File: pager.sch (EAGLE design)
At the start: 62 parts, among them Q1 25 MHz, Q2 SI2333DS, SW1 CHS-01A1, SW2 CHS-01A1, U1 VOCORE2SMD, U2 VOCORE2SMD, U3 XR22800IL, X1 52745-3090

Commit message: Fixed some parts, better placement
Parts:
- C11: value 18 pF -> 4.7 uF cer; device pager:CAP_CERAMIC_0402 -> pager:CAP_CERAMIC_0603
- C9: value 4.7 uF cer -> 18 pF; device pager:CAP_CERAMIC_0603 -> pager:CAP_CERAMIC_0402
- R1, R10, R25: value 50 -> 10 k
- R17: value 226 -> 50
- R18: value 1M -> 50
- R19: value 40.2k -> 50
- R20: value 10 k -> 50
- R36: value 50 -> 1M
- R37: value 10 k -> 226
- R38: value 10 k -> 40.2k
- U1, U2: value VOCORE2SMD -> VOCORE2-SMD; device pager:VOCORE2SMD -> pager:VOCORE2-SMD
- X1: value 52745-3090 -> OMRON_XF2L-30REVERSE; device pager:52745-3090 -> pager:OMRON_XF2L-30REVERSE
- X2: value (none) -> FCI_8193_MICRO_USB; device pager:USB"" -> pager:FCI_8193_MICRO_USB
- renumbered WP_CORE to TP2, WP_WIFI to TP1
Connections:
- removed net BIAS_1B: C9.1, U3.+3.3V_OUT, U3.CAP1, U3.CAP2
- removed net N$26: X2.GND
- new net 3.3V_USB: C11.1, U3.+3.3V_OUT, U3.CAP1, U3.CAP2
- net +5V: now also C13.1; no longer C12.1, U1.+5.0VI_2, U2.+5.0VI_2
- net 3.3_CORE: now also R13.2, R15.2, R17.2, R19.2, R21.2, R23.2, R26.2, U2.+3.3VO; no longer R1.2, R10.2, R12.2, R2.2, R3.2, R4.2, R9.2, U1.+3.3VO, U1.+3.3VO_2, U1.+3.3VO_3
- net 3.3_WIFI: now also R2.2, R4.2, R6.2, R8.2, U1.+3.3VO; no longer R13.2, R14.2, R15.2, R16.2, U2.+3.3VO, U2.+3.3VO_2, U2.+3.3VO_3
- net DISP_RESET: now also R25.2, U2.(GPIO#39)EPHY_LED4_N_JTRST_N; no longer R20.2, U1.(GPIO#39)EPHY_LED4_N_JTRST_N
- net DISP_RX0: now also U2.(GPIO#45,PWM_CH0)UART_TXD1; no longer U1.(GPIO#45,PWM_CH0)UART_TXD1
- net DISP_TX0: now also U2.(GPIO#46,PWM_CH1)UART_RXD1; no longer U1.(GPIO#46,PWM_CH1)UART_RXD1
- net ETH_1A_RX_N: now also C8.1, R19.1, R20.2, U2.MDI_RN_P0; no longer C4.1, R21.2, R4.1, U1.MDI_RN_P0
- net ETH_1A_RX_P: now also C7.1, R21.1, U2.MDI_RP_P0; no longer C3.1, R3.1, U1.MDI_RP_P0
- net ETH_1A_TX_N: now also C6.1, R23.1, R24.2, U2.MDI_TN_P0; no longer C2.1, R2.1, R23.2, U1.MDI_TN_P0
- net ETH_1A_TX_P: now also C5.1, R26.1, R27.2, U2.MDI_TP_P0; no longer C1.1, R1.1, R24.2, U1.MDI_TP_P0
- net ETH_1B_RX_N: now also C6.2, R30.1, R31.2; no longer C2.2, R26.2, R6.1
- net ETH_1B_RX_P: now also C5.2, R28.1, R29.2; no longer C1.2, R25.2, R5.1
- net ETH_1B_TX_N: now also C8.2, R34.1, R35.2; no longer C4.2, R28.2, R8.1
- net ETH_1B_TX_P: now also C7.2, R32.1, R33.2; no longer C3.2, R27.2, R7.1
- net ETH_2A_RX_N: now also C4.1, R17.1, R18.2, U2.(PWM_CH1,GPIO#19,SD_D6)MDI_RN_P2; no longer C8.1, R12.1, R32.2, U1.(PWM_CH1,GPIO#19,SD_D6)MDI_RN_P2
- net ETH_2A_RX_P: now also C3.1, R15.1, R16.2, U2.(PWM_CH0,GPIO#18,SD_D7)MDI_RP_P2; no longer C7.1, R11.1, R31.2, U1.(PWM_CH0,GPIO#18,SD_D7)MDI_RP_P2
- net ETH_2A_TX_N: now also C2.1, R13.1, R14.2, U2.(UART_RXD2,GPIO#21,PWM_CH3,SD_D4)MDI_TN_P2; no longer C6.1, R10.1, R30.2, U1.(UART_RXD2,GPIO#21,PWM_CH3,SD_D4)MDI_TN_P2
- net ETH_2A_TX_P: now also C1.1, R11.1, R12.2, U2.(UART_TXD2,GPIO#20,PWM_CH2,SD_D5)MDI_TP_P2; no longer C5.1, R29.2, R9.1, U1.(UART_TXD2,GPIO#20,PWM_CH2,SD_D5)MDI_TP_P2
- net ETH_2B_RX_N: now also C2.2, R6.1, R7.2, U1.MDI_RN_P0; no longer C6.2, R14.1, R35.2, U2.MDI_RN_P0
- net ETH_2B_RX_P: now also C1.2, R8.1, R9.2, U1.MDI_RP_P0; no longer C5.2, R13.1, R36.2, U2.MDI_RP_P0
- net ETH_2B_TX_N: now also C4.2, R2.1, R3.2, U1.MDI_TN_P0; no longer C8.2, R16.1, R33.2, U2.MDI_TN_P0
- net ETH_2B_TX_P: now also C3.2, R4.1, R5.2, U1.MDI_TP_P0; no longer C7.2, R15.1, R34.2, U2.MDI_TP_P0
- net GND: now also C11.2, C13.2, C9.1, R1.1, R10.1, R12.1, R14.1, R16.1, R18.1, R3.1, R5.1, R7.1, R9.1, X2.GND; no longer C11.1, C12.2, C9.2, R17.1, R19.1, R21.1, R23.1, R26.1, R28.1, R30.1, R32.1, R34.1, R36.1, U1.GND_2, U1.GND_3, U1.GND_4, U1.GND_5, U1.GND_6, U1.GND_7, U2.GND_2, U2.GND_3, U2.GND_4, U2.GND_5, U2.GND_6, U2.GND_7
- net N$10: now also R28.2, R30.2, R32.2, R34.2; no longer R5.2, R6.2, R7.2, R8.2
- net N$21: now also R37.2; no longer R17.2
- net N$22: now also C10.2, R36.2; no longer C11.2, R18.2
- net N$23: now also C9.2, R36.1; no longer C10.2, R18.1
- net N$27: now also C12.1; no longer C13.1
- net N$28: now also C12.2, R38.2; no longer C13.2, R19.2
- net WP_CORE: now also R10.2; no longer R38.2
- net WP_WIFI: now also R1.2; no longer R37.2
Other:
- moved on the sheet: C1, C10, C11, C12, C13, C2, C3, C4, C5, C6, C7, C8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

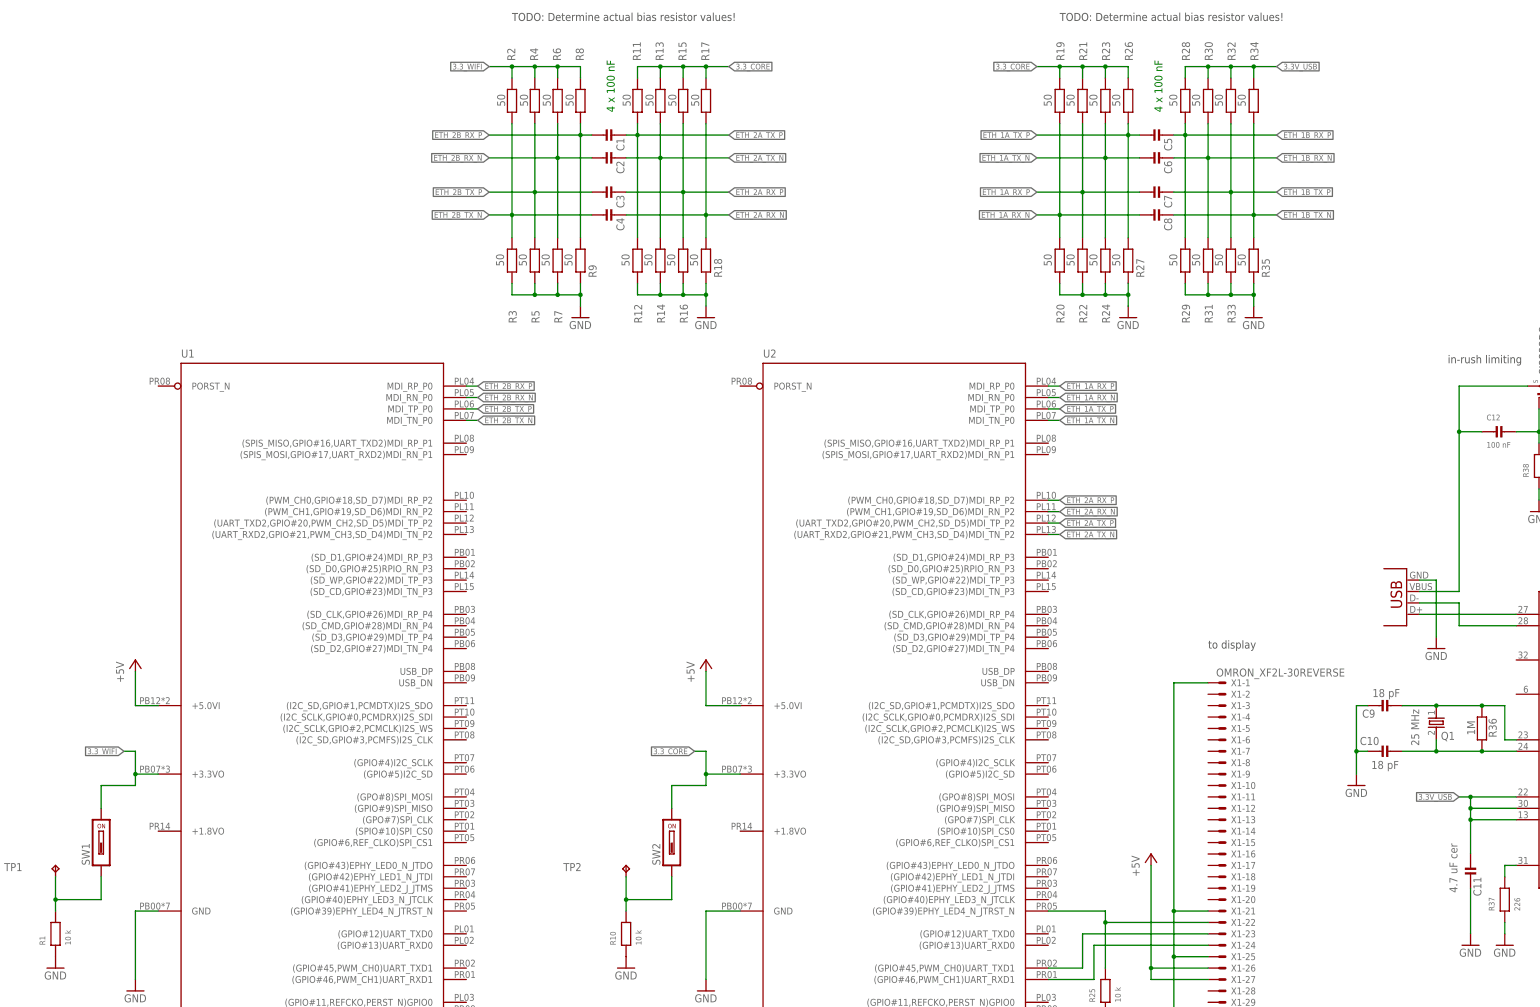
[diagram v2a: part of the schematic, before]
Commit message: Added wifi_reset wire, polygons on tRestrict for Vocore's and routed power bus and USB
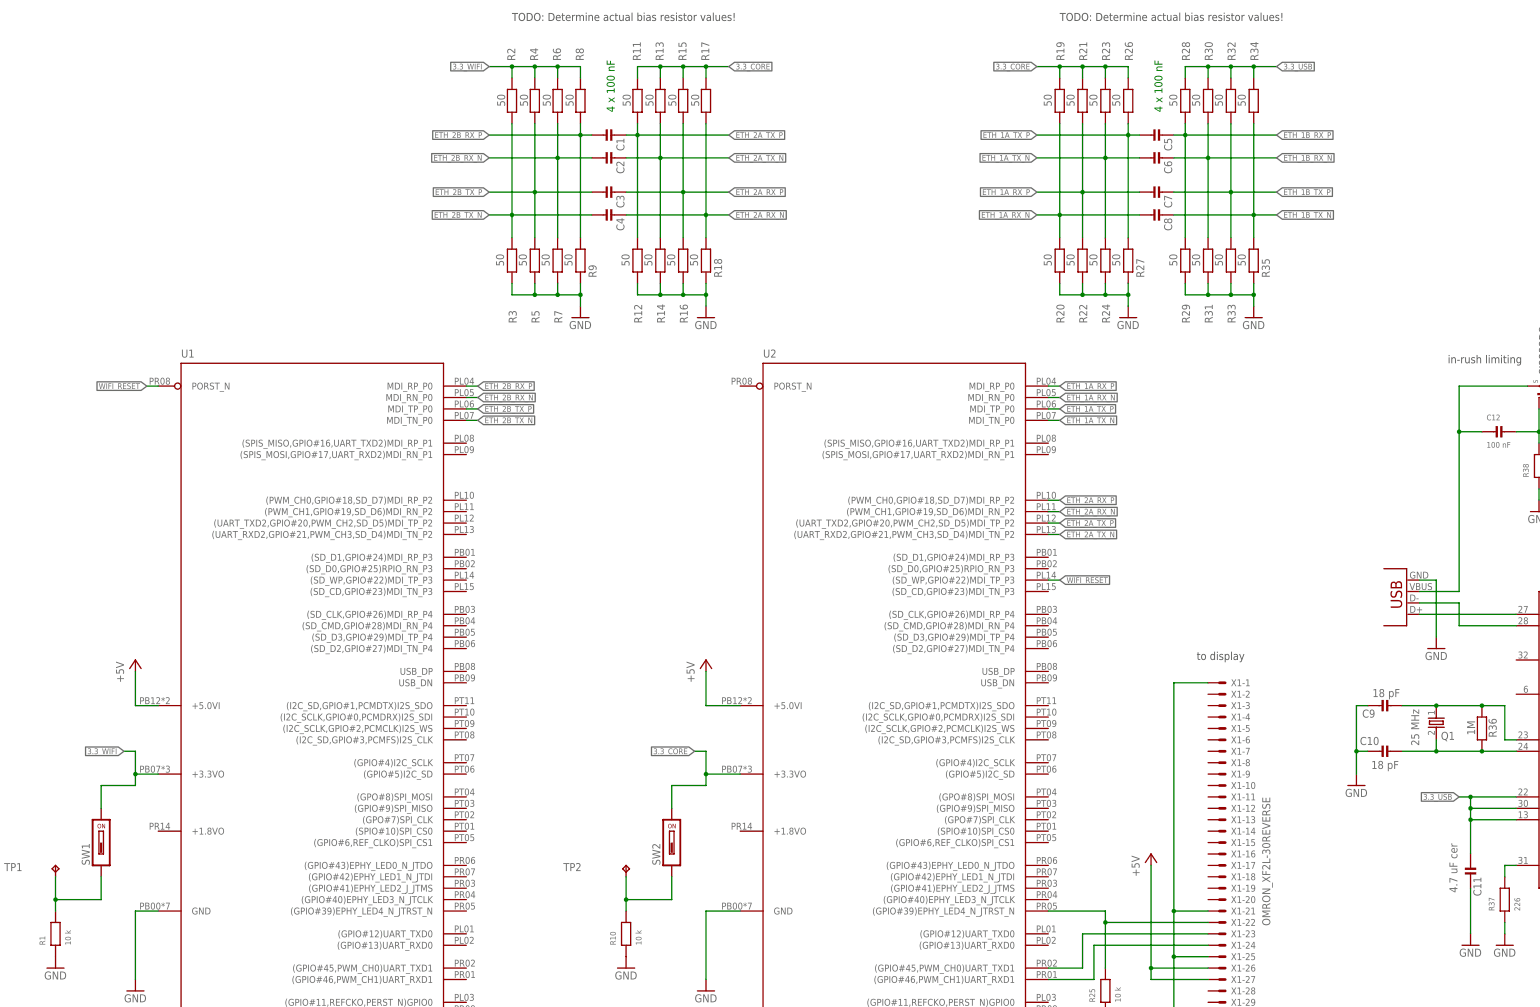
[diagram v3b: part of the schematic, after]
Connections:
- removed net 3.3V_USB: C11.1, U3.+3.3V_OUT, U3.CAP1, U3.CAP2
- removed net N$10: R28.2, R30.2, R32.2, R34.2
- new net 3.3_USB: C11.1, R28.2, R30.2, R32.2, R34.2, U3.+3.3V_OUT, U3.CAP1, U3.CAP2
- new net WIFI_RESET: U1.PORST_N, U2.(SD_WP,GPIO#22)MDI_TP_P3

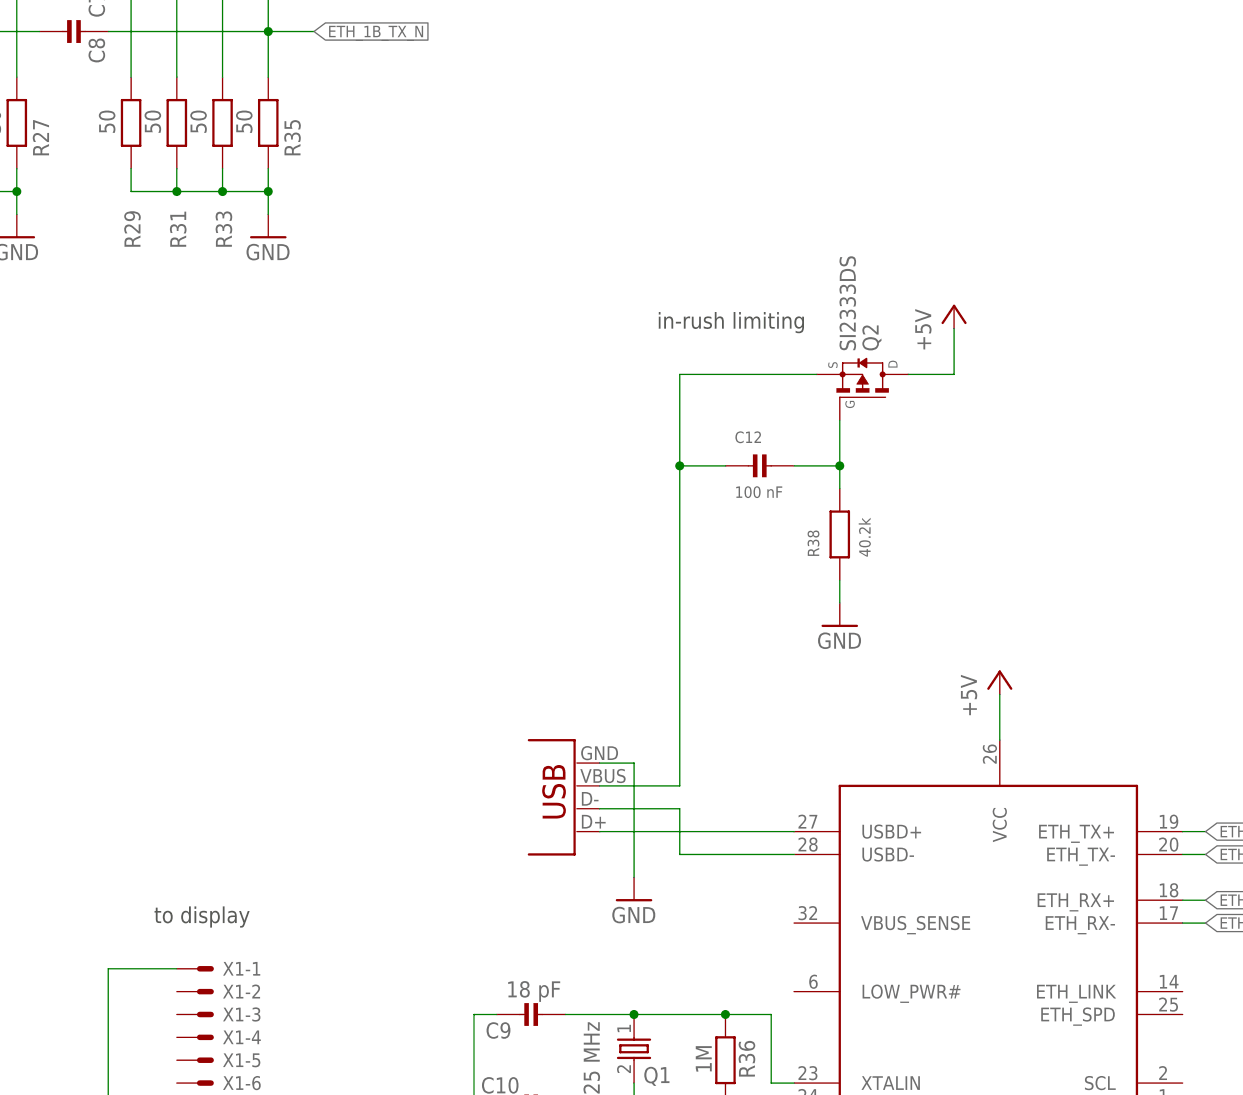
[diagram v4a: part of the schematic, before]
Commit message: Added TVS, resistor and cap between USB-shield and GND, made +5V bus 0.8 mm thick
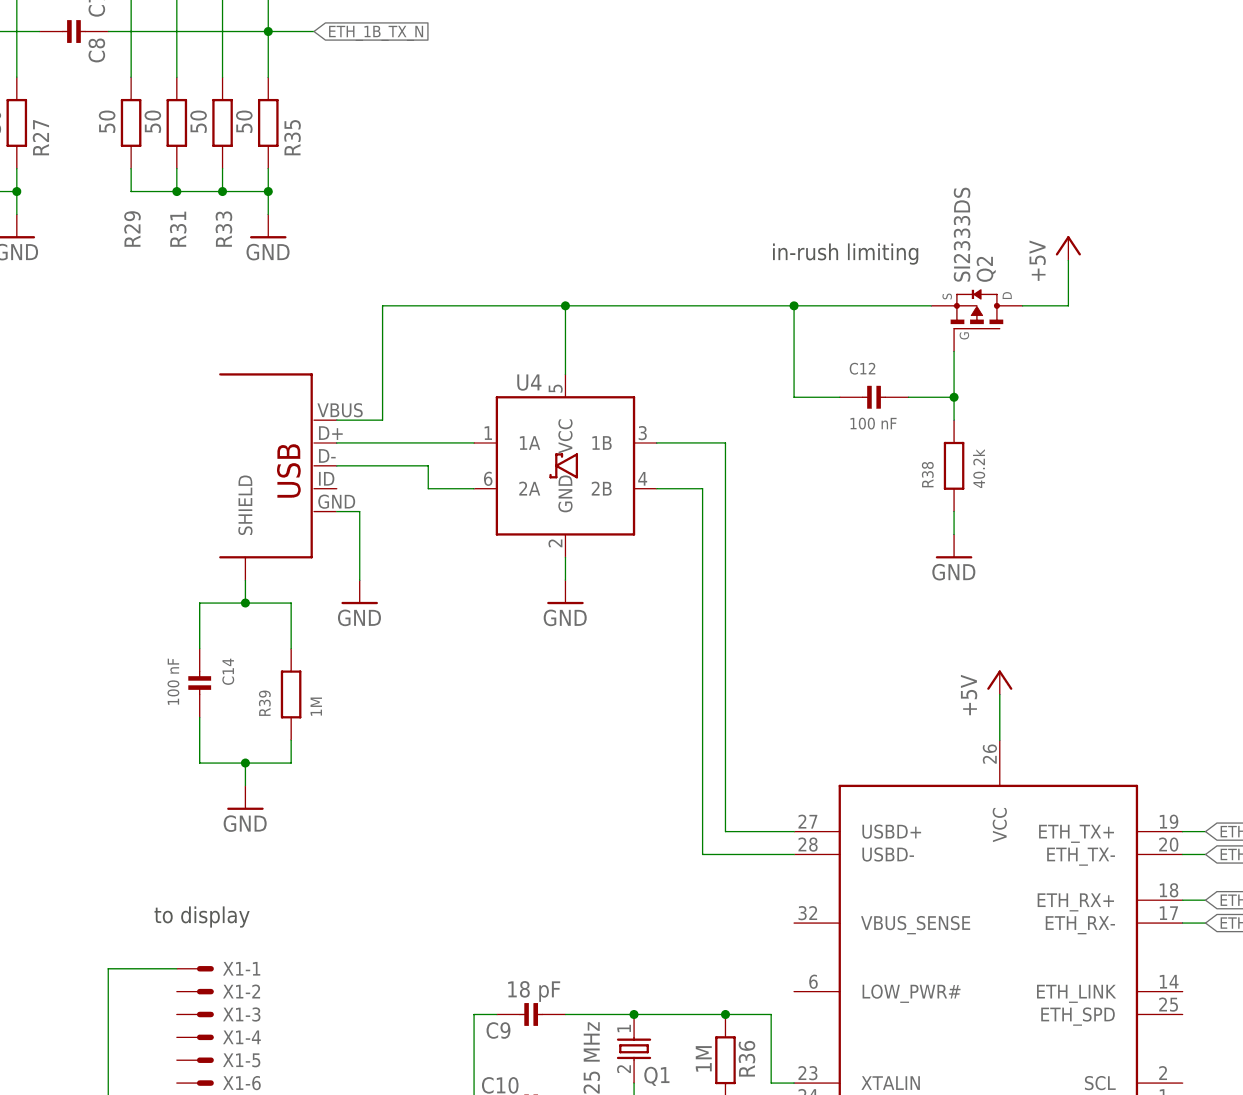
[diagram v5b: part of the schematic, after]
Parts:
- added C14: 100 nF, pager:CAP_CERAMIC_0402
- added R39: 1M, pager:RESISTOR_0402
- added U4: IP4234CZ6, pager:IP4234CZ6
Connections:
- removed net N$27: C12.1, Q2.S, X2.VBUS
- removed net USB_D_N: U3.USBD-, X2.D-
- removed net USB_D_P: U3.USBD+, X2.D+
- new net RAW_+5V: C12.1, Q2.S, U4.VCC, X2.VBUS
- new net SHIELD: C14.1, R39.2, X2.SHIELD
- new net USB_N: U3.USBD-, U4.2B
- new net USB_P: U3.USBD+, U4.1B
- new net USB_RAW_N: U4.2A, X2.D-
- new net USB_RAW_P: U4.1A, X2.D+
- net GND: now also C14.2, R39.1, U4.GND
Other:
- moved on the sheet: C12, Q2, R38

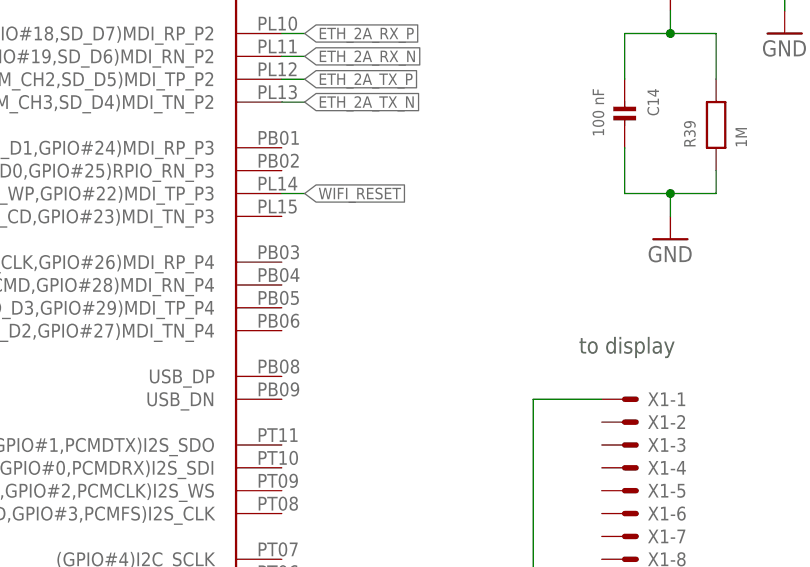
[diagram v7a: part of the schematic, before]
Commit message: placed R40 to pull down wifi-reset
Not sure whether good idea, it's a trade-off. We can always not
populate.
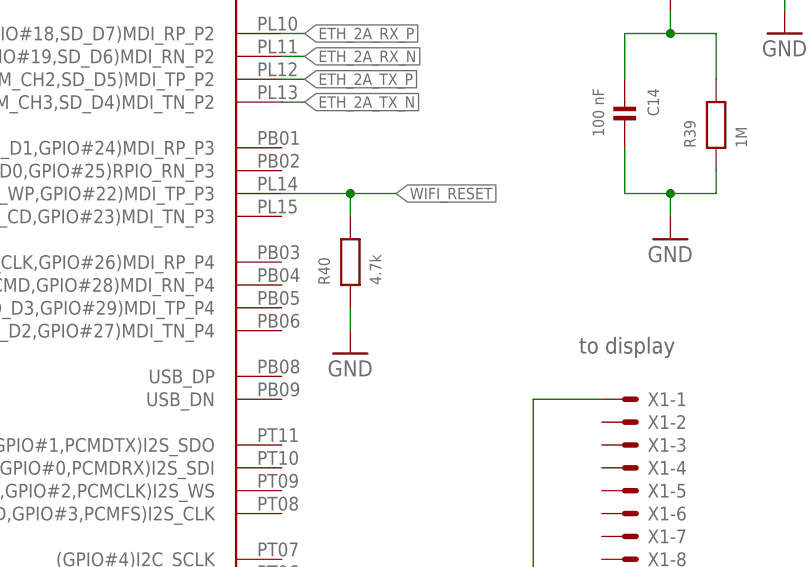
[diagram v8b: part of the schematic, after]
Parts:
- added R40: 4.7k, pager:RESISTOR_0402
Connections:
- net GND: now also R40.1
- net WIFI_RESET: now also R40.2
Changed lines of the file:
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@@
 <part name="R39" library="pager" deviceset="RESISTOR" device="_0402" value="1M"/>
 <part name="GND19" library="pager" deviceset="GND" device=""/>
+<part name="R40" library="pager" deviceset="RESISTOR" device="_0402" value="4.7k"/>
+<part name="GND20" library="pager" deviceset="GND" device=""/>
 </parts>
 <sheets>
@@
 <instance part="R39" gate="G$1" x="81.28" y="55.88" rot="R90"/>
 <instance part="GND19" gate="1" x="76.2" y="43.18"/>
+<instance part="R40" gate="G$1" x="40.64" y="40.64" rot="R90"/>
+<instance part="GND20" gate="1" x="40.64" y="30.48"/>
 </instances>
 <busses>
@@
 <junction x="76.2" y="48.26"/>
 </segment>
+<segment>
+<pinref part="R40" gate="G$1" pin="1"/>
+<pinref part="GND20" gate="1" pin="GND"/>
+<wire x1="40.64" y1="35.56" x2="40.64" y2="33.02" width="0.1524" layer="91"/>
+</segment>
 </net>
 <net name="ETH_1B_TX_P" class="1">
@@
 <segment>
 <pinref part="U2" gate="G$1" pin="(SD_WP,GPIO#22)MDI_TP_P3"/>
-<wire x1="33.02" y1="48.26" x2="35.56" y2="48.26" width="0.1524" layer="91"/>
-<label x="35.56" y="48.26" size="1.27" layer="95" xref="yes"/>
-</segment>
-</net>
+<wire x1="33.02" y1="48.26" x2="40.64" y2="48.26" width="0.1524" layer="91"/>
+<label x="45.72" y="48.26" size="1.27" layer="95" xref="yes"/>
+<pinref part="R40" gate="G$1" pin="2"/>
+<wire x1="40.64" y1="48.26" x2="45.72" y2="48.26" width="0.1524" layer="91"/>
+<wire x1="40.64" y1="45.72" x2="40.64" y2="48.26" width="0.1524" layer="91"/>
+<junction x="40.64" y="48.26"/>
+</segment>
+</net>
